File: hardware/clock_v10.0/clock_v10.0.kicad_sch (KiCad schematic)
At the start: 217 parts, among them J1 RJ45, J14 DC-005B-2.5A-2.0, J2 Conn_01x03, J4 USB_C_Receptacle, J5 Conn_01x06_Pin, Q1 2N7002, Q10 2N7002, Q9 2N7002, SW1 SW_Push_4PDT, U1 ADA4807-1, U10 STM32F405RGTx, U11 AMS1117-3.3, U12 BA50DD0WHFP-TR, U13 M24C02-RMN, U14 CH340C, U15 USBLC6-2P6, U16 TLV3603DCKR, U17 SN74LVC1G14DBV, U18 TMP112AIDRLR, U19 SN74LVC1G14DBV, U2 SN74LVC1G14DBV, U20 SN74LVC1G14DBV, U21 SN74LVC1G14DBV, U23 TPS63060, U3 SN74LVC1G14DBV, U4 ADA4807-1, U5 ADA4807-1, U6 TLV3603DCKR, U7 SN74LVC1G14DBV, U8 TLV3603DCKR, U9 L78L05_SOT89, Y1 AOCJY4A-10.000MHZ-SW, Y2 16MHz

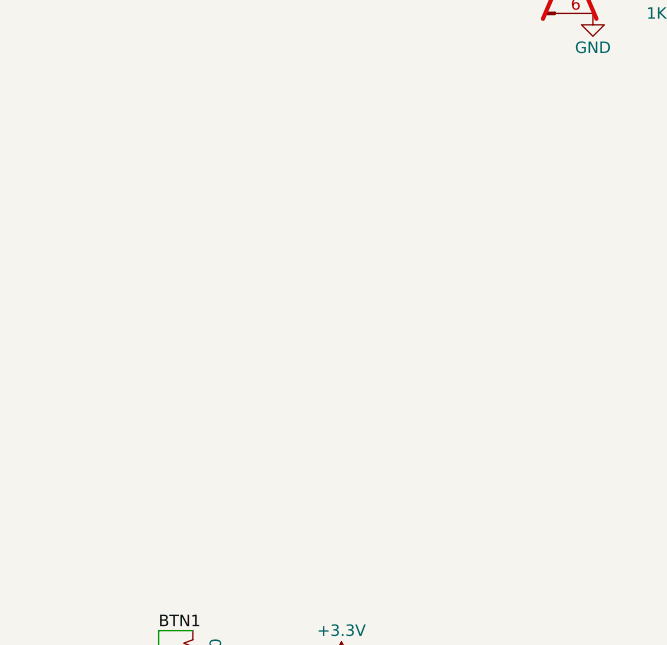
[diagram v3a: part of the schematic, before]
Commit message: Add PP/LTC Jumper Fixes #275
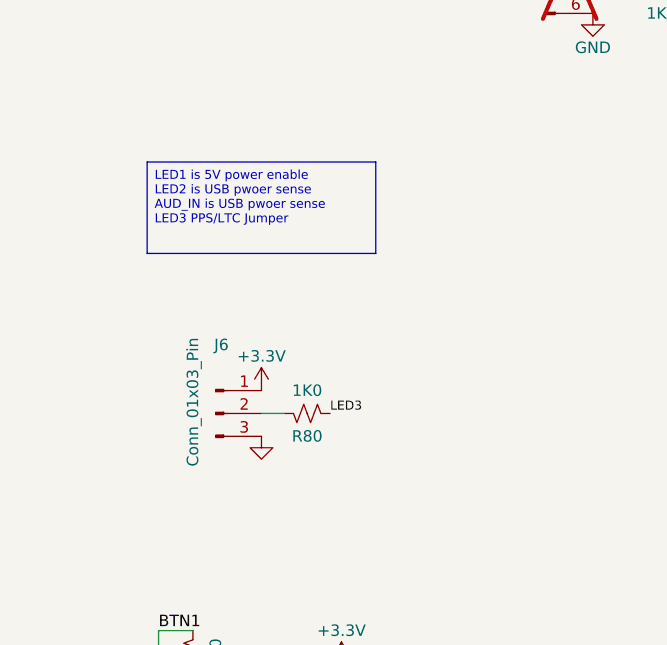
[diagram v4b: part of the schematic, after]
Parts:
- added J6: Conn_01x03_Pin, Connector_PinHeader_2.54mm:PinHeader_1x03_P2.54mm_Vertical, symbol Connector:Conn_01x03_Pin
- added R80: 1K0, Resistor_SMD:R_0603_1608Metric, symbol Device:R_Small_US
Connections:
- net +3.3V: now also J6.1 (Pin_1)
- net GND: now also J6.3 (Pin_3)
- net LED3: now also R80.1
- new net: J6.2 (Pin_2), R80.2
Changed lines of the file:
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@@
     (stroke (width 0) (type default))
   )
+  (wire (pts (xy 52.07 144.78) (xy 49.53 144.78))
+    (stroke (width 0) (type default))
+  )
   (wire (pts (xy 143.51 363.22) (xy 143.51 367.03))
     (stroke (width 0) (type default))
@@
     (stroke (width 0) (type default))
   )
+  (text_box "LED1 is 5V power enable\nLED2 is USB pwoer sense\nAUD_IN is USB pwoer sense \nLED3 PPS/LTC Jumper "
+    (at 36.83 116.84 0) (size 25.4 10.16)
+    (stroke (width 0) (type default))
+    (fill (type none))
+    (effects (font (size 1 1)) (justify left top))
+  )
   (text "Mounting Holes" (at 113.03 41.91 0)
     (effects (font (size 1.27 1.27)) (justify right bottom))
@@
     (effects (font (size 1.27 1.27)) (justify left bottom))
   )
+  (label "LED3" (at 57.15 144.78 0) (fields_autoplaced)
+    (effects (font (size 1 1)) (justify left bottom))
+  )
   (label "AUX_SYNC_IN" (at 177.8 71.12 180) (fields_autoplaced)
     (effects (font (size 1.27 1.27)) (justify right bottom))
@@
     )
   )
+  (symbol (lib_id "power:GND") (at 49.53 147.32 0) (mirror y) (unit 1)
+    (in_bom yes) (on_board yes) (dnp no)
+    (property "Reference" "#PWR042" (at 49.53 153.67 0)
+      (effects (font (size 1.27 1.27)) hide)
+    )
+    (property "Value" "GND" (at 46.99 149.86 0)
+      (effects (font (size 1.27 1.27)) hide)
+    )
+    (property "Footprint" "" (at 49.53 147.32 0)
+      (effects (font (size 1.27 1.27)) hide)
+    )
+    (property "Datasheet" "" (at 49.53 147.32 0)
+      (effects (font (size 1.27 1.27)) hide)
+    )
+    (pin "1")
+    (instances
+      (project "clock_v10.0"
+        (path "/bd4d3b9a-07c1-4a53-9c94-2893f3e869d4"
+          (reference "#PWR042") (unit 1)
+        )
+      )
+    )
+  )
   (symbol (lib_id "Device:C_Small") (at 271.78 85.09 0) (unit 1)
     (in_bom yes) (on_board yes) (dnp no)
@@
     )
   )
+  (symbol (lib_id "Connector:Conn_01x03_Pin") (at 44.45 144.78 0) (unit 1)
+    (in_bom yes) (on_board yes) (dnp no)
+    (property "Reference" "J6" (at 45.085 137.16 0)
+      (effects (font (size 1.27 1.27)))
+    )
+    (property "Value" "Conn_01x03_Pin" (at 41.91 143.51 90)
+      (effects (font (size 1.27 1.27)))
+    )
+    (property "Footprint" "Connector_PinHeader_2.54mm:PinHeader_1x03_P2.54mm_Vertical" (at 44.45 144.78 0)
+      (effects (font (size 1.27 1.27)) hide)
+    )
+    (property "Datasheet" "~" (at 44.45 144.78 0)
+      (effects (font (size 1.27 1.27)) hide)
+    )
+    (pin "1")
+    (pin "2")
+    (pin "3")
+    (instances
+      (project "clock_v10.0"
+        (path "/bd4d3b9a-07c1-4a53-9c94-2893f3e869d4"
+          (reference "J6") (unit 1)
+        )
+      )
+    )
+  )
   (symbol (lib_id "Device:R_Small_US") (at 242.57 67.31 0) (unit 1)
     (in_bom yes) (on_board yes) (dnp no) (fields_autoplaced)
@@
     )
   )
+  (symbol (lib_id "power:+3.3V") (at 49.53 142.24 0) (mirror y) (unit 1)
+    (in_bom yes) (on_board yes) (dnp no) (fields_autoplaced)
+    (property "Reference" "#PWR0109" (at 49.53 146.05 0)
+      (effects (font (size 1.27 1.27)) hide)
+    )
+    (property "Value" "+3.3V" (at 49.53 138.43 0)
+      (effects (font (size 1.27 1.27)))
+    )
+    (property "Footprint" "" (at 49.53 142.24 0)
+      (effects (font (size 1.27 1.27)) hide)
+    )
+    (property "Datasheet" "" (at 49.53 142.24 0)
+      (effects (font (size 1.27 1.27)) hide)
+    )
+    (pin "1")
+    (instances
+      (project "clock_v10.0"
+        (path "/bd4d3b9a-07c1-4a53-9c94-2893f3e869d4"
+          (reference "#PWR0109") (unit 1)
+        )
+      )
+    )
+  )
   (symbol (lib_id "Device:R_Small_US") (at 82.55 252.73 270) (unit 1)
     (in_bom yes) (on_board yes) (dnp no)
@@
         )
       )
+    )
+  )
+  (symbol (lib_id "Device:R_Small_US") (at 54.61 144.78 270) (mirror x) (unit 1)
+    (in_bom yes) (on_board yes) (dnp no)
+    (property "Reference" "R80" (at 54.61 147.32 90)
+      (effects (font (size 1.27 1.27)))
+    )
+    (property "Value" "1K0" (at 54.61 142.24 90)
+      (effects (font (size 1.27 1.27)))
+    )
+    (property "Footprint" "Resistor_SMD:R_0603_1608Metric" (at 54.61 144.78 0)
+      (effects (font (size 1.27 1.27)) hide)
+    )
+    (property "Datasheet" "~" (at 54.61 144.78 0)
+      (effects (font (size 1.27 1.27)) hide)
+    )
+    (property "JLCPCB Part #" "C21190" (at 54.61 144.78 0)
+      (effects (font (size 1.27 1.27)) hide)
+    )
+    (pin "1")
+    (pin "2")
+    (instances
+      (project "clock_v10.0"
+        (path "/bd4d3b9a-07c1-4a53-9c94-2893f3e869d4"
+          (reference "R80") (unit 1)
+        )
+      )

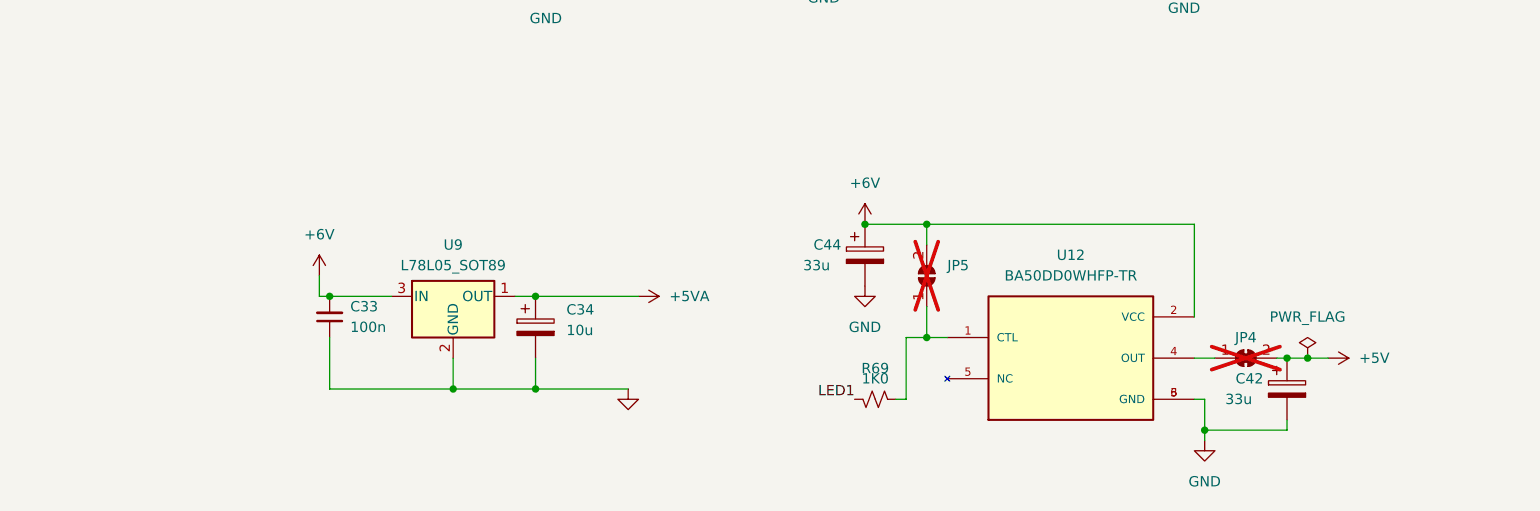
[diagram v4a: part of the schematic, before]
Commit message: add power sense resisitors Fixes #294
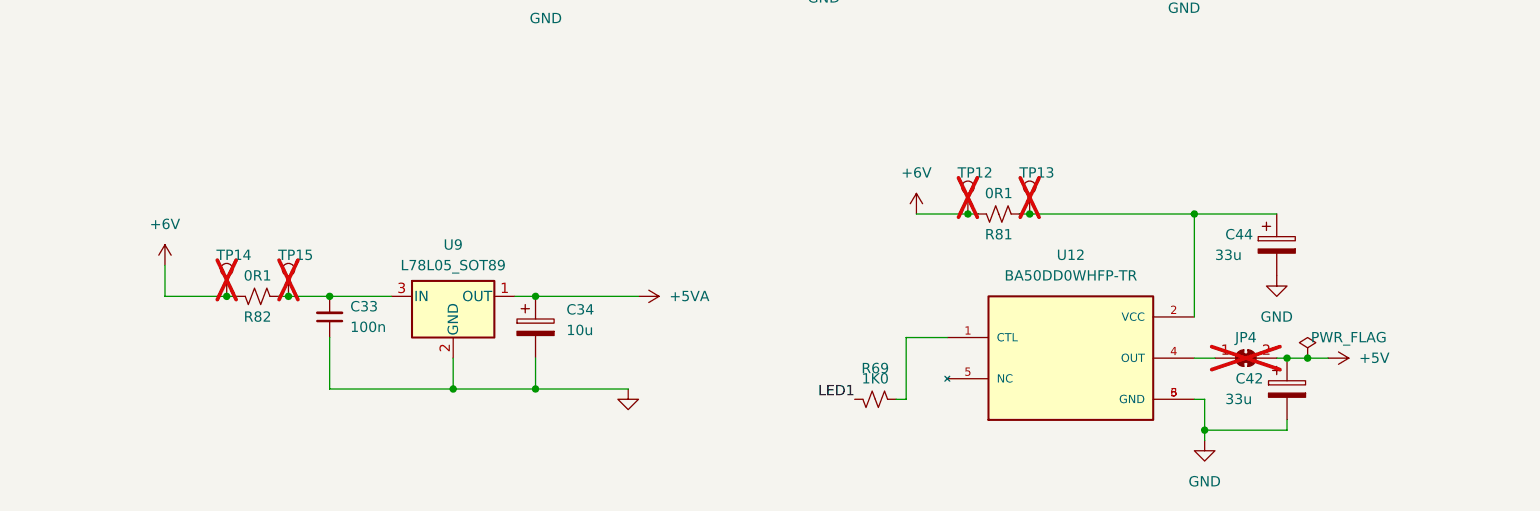
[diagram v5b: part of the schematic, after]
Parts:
- removed JP5: SolderJumper_2_Open, Jumper:SolderJumper-2_P1.3mm_Open_RoundedPad1.0x1.5mm, symbol Jumper:SolderJumper_2_Open
- added R81, R82: 0R1, Resistor_SMD:R_1206_3216Metric, symbol Device:R_Small_US
- added TP12, TP13, TP14, TP15: ~, TestPoint:TestPoint_THTPad_D1.0mm_Drill0.5mm, symbol Connector:TestPoint
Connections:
- net +6V: now also R81.2, R82.2, TP12.1, TP14.1; no longer C33.2, C44.1, U12.2 (VCC), U9.3 (IN)
- new net: C44.1, R81.1, TP13.1, U12.2 (VCC)
- new net: C33.2, R82.1, TP15.1, U9.3 (IN)
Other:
- moved on the sheet: C44

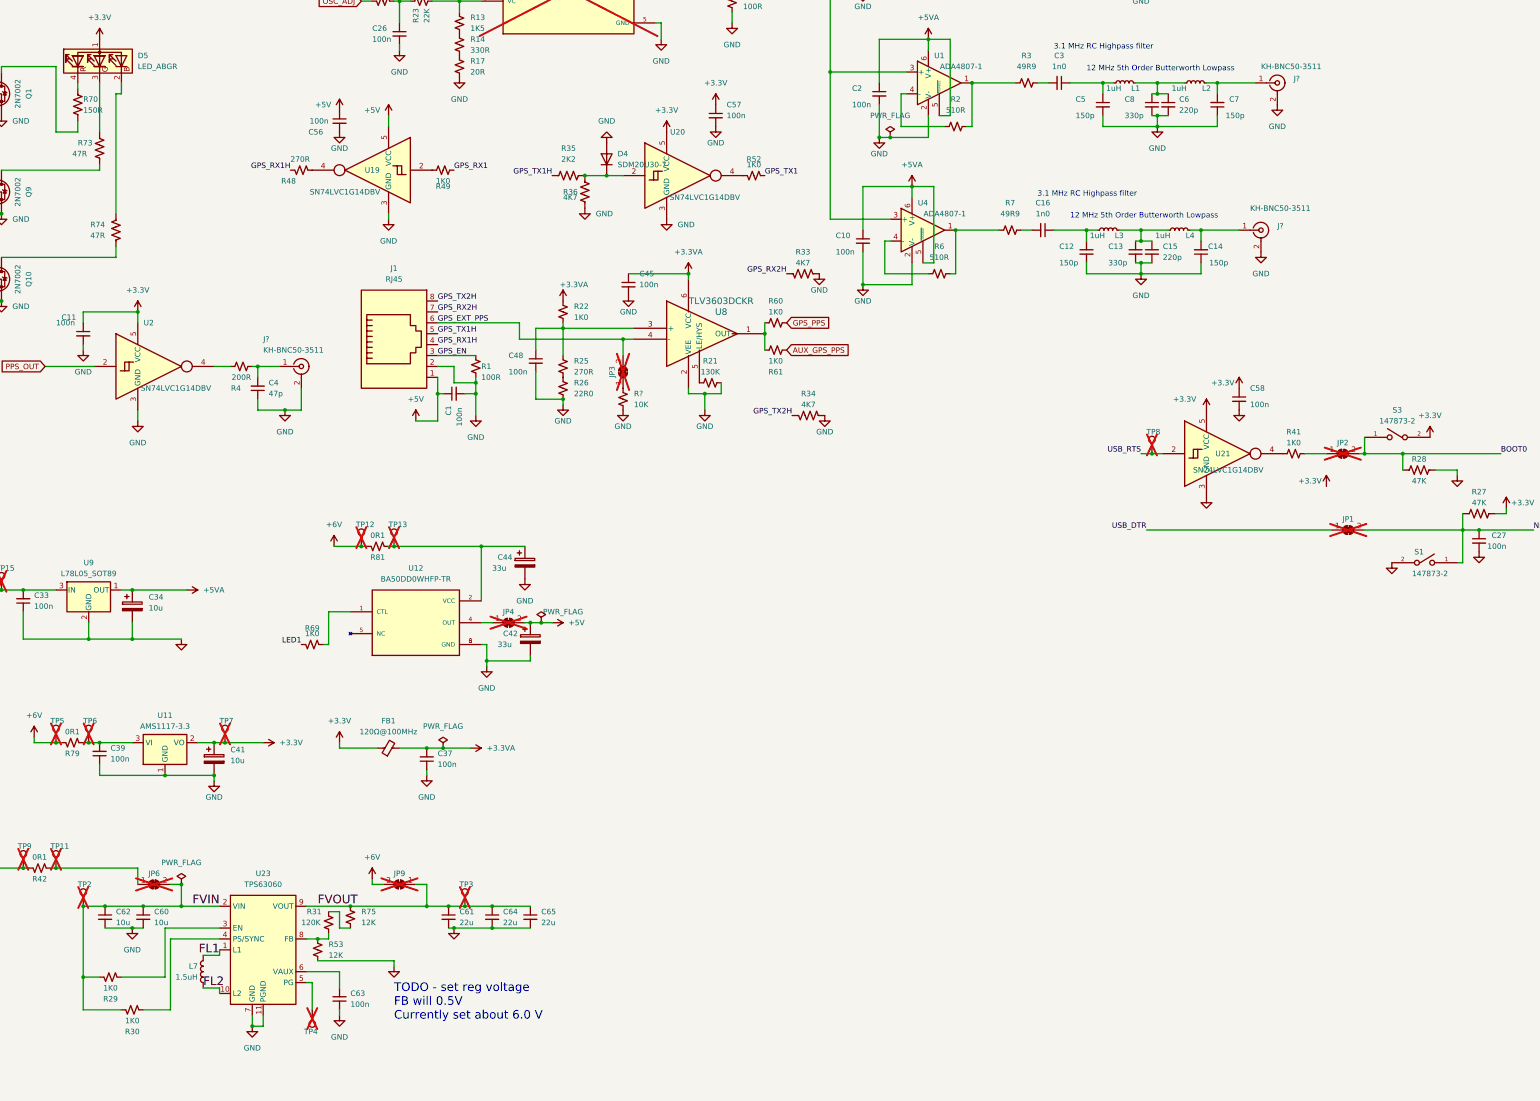
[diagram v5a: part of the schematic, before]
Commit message: add jumper for USB / Reset disconnect Fixes #293
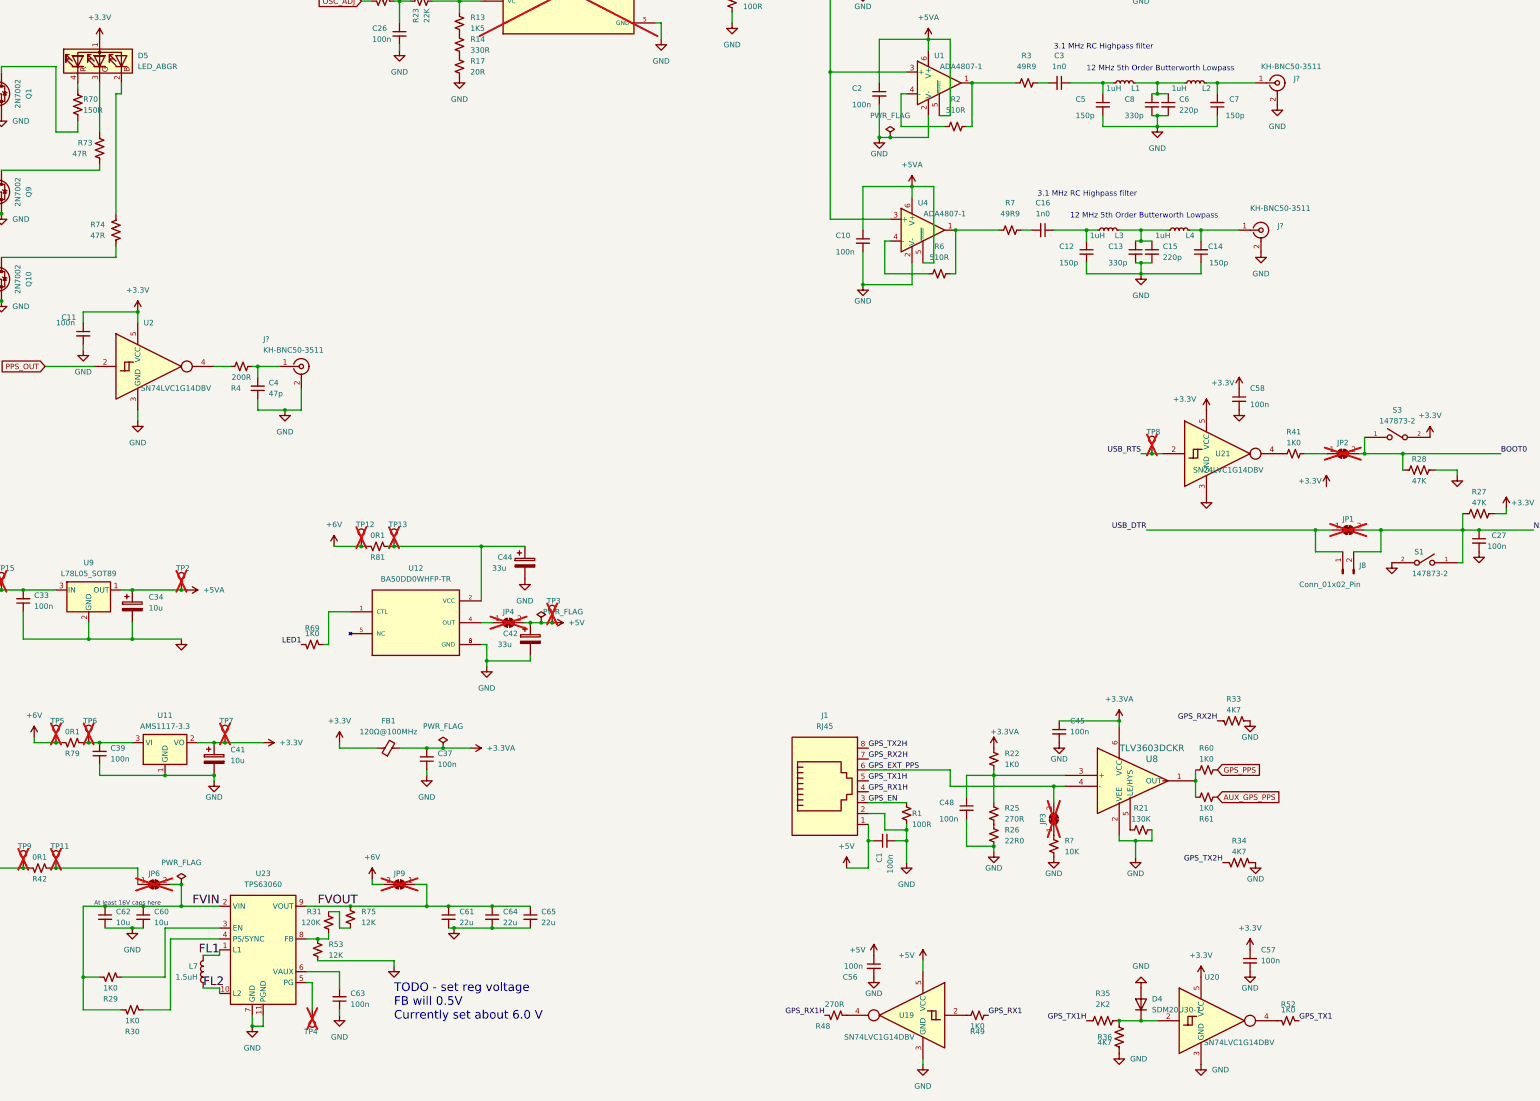
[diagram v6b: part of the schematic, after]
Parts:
- added J8: Conn_01x02_Pin, Connector_PinHeader_2.54mm:PinHeader_1x02_P2.54mm_Vertical, symbol Connector:Conn_01x02_Pin
- TP2, TP3: footprint TestPoint:TestPoint_THTPad_D1.5mm_Drill0.7mm -> TestPoint:TestPoint_THTPad_D1.0mm_Drill0.5mm
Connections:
- net +5V: now also TP3.1
- net +5VA: now also TP2.1
- net FVIN: no longer TP2.1
- net FVOUT: no longer TP3.1
- net NRST: now also J8.2 (Pin_2)
- net USB_DTR: now also J8.1 (Pin_1)
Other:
- note added: "At least 16V caps here"
- moved on the sheet: C1, C45, C48, C56, C57, D4, J1, JP3, R1, R21, R22, R25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
